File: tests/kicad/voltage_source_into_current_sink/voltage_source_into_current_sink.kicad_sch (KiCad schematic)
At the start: 2 parts

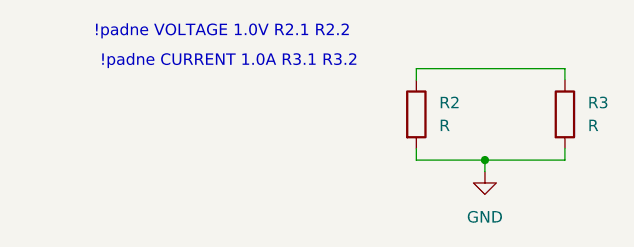
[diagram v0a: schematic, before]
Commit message: feat: Richer directive syntax
This commit adds support for named directive parameters. No more
guessing which parameter is the positive terminal positive and which is the
negative terminal!
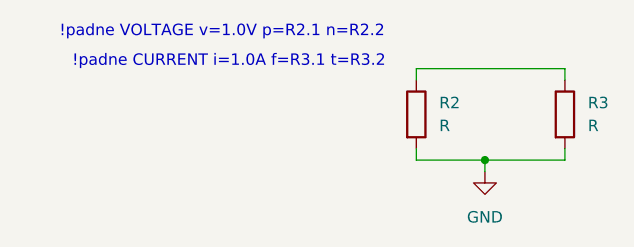
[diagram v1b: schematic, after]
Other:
- note added: "!padne CURRENT i=1.0A f=R3.1 t=R3.2"
- note added: "!padne VOLTAGE v=1.0V p=R2.1 n=R2.2"
- note removed: "!padne CURRENT 1.0A R3.1 R3.2"
- note removed: "!padne VOLTAGE 1.0V R2.1 R2.2"
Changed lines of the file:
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@@
 		)
 	)
-	(text "!padne VOLTAGE 1.0V R2.1 R2.2"
+	(text "!padne VOLTAGE v=1.0V p=R2.1 n=R2.2"
 		(exclude_from_sim no)
 		(at 118.11 96.266 0)
@@
 		)
 	)
-	(text "!padne CURRENT 1.0A R3.1 R3.2"
+	(text "!padne CURRENT i=1.0A f=R3.1 t=R3.2"
 		(exclude_from_sim no)
 		(at 118.872 99.568 0)
